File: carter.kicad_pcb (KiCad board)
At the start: 2 copper layers, 45 x 41 mm, 14 parts, among them J1 USB C, J2 Micro_SD_Card, U1 CH340C

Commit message: near v1
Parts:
- added C2: 0.1uF, Capacitor_SMD:C_0603_1608Metric, F.Cu at (148.7, 87.5)
- R3, R4, R5, R6, R7: footprint Resistor_SMD:R_0603_1608Metric -> Resistor_SMD:R_0805_2012Metric
- R8: value R -> 220
- U2: footprint LeapFrog:LeapFrog-Cart -> LeapFrog:Cartridge
- moved U2 42.5 mm to (152.5, 55.0)
- moved D1 36.1 mm to (153.7, 97.0)
- moved J1 34.5 mm to (141.3, 96.9), turned to 0 degrees
- moved R2 33.5 mm to (135.0, 90.0), turned to 180 degrees
- moved C1 26.4 mm to (141.8, 80.0), turned to 180 degrees
- moved J2 23.3 mm to (163.2, 89.8), turned to 0 degrees
- moved R1 21.9 mm to (147.6, 90.0)
- moved R8 11.0 mm to (149.7, 97.0)
- moved R3 10.3 mm to (170.5, 77.5), turned to 180 degrees
- moved U1 10.3 mm to (141.8, 85.0)
- moved R4 9.23 mm to (166.4, 76.5), turned to 180 degrees
- moved R5 7.98 mm to (165.4, 80.0), turned to 180 degrees
- moved R6 7.24 mm to (159.6, 77.5)
- moved R7 5.76 mm to (158.2, 81.2)
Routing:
- net GND: track 0.00 -> 43.7 mm, vias 0 -> 14
- net /SD_D0: track 0.00 -> 35.2 mm
- net /SD_D3: track 0.00 -> 32.2 mm
- net /SD_D2: track 0.00 -> 30.8 mm, vias 0 -> 2
- net /SD_CMD: track 0.00 -> 30.6 mm
- net /SD_CLK: track 0.00 -> 29.9 mm
- net /SD_D1: track 0.00 -> 29.7 mm
- net +3V3: track 0.00 -> 17.4 mm
- net Net-(J1-CC1): track 0.00 -> 6.72 mm
- net Net-(J1-CC2): track 0.00 -> 6.40 mm
- net Net-(U1-UD+): track 8.83 -> 12.5 mm
- net Net-(D1-K): track 0.00 -> 2.43 mm
- net Net-(U1-TXD): track 31.3 -> 33.0 mm
- net Net-(U1-RXD): track 31.3 -> 33.0 mm
- net Net-(U1-UD-): track 12.0 -> 11.0 mm
- added copper zone on F.Cu, net +3V3
- removed copper zone on F.Cu, net GND
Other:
- board size 45 x 41 mm -> 45 x 50 mm
- board text added: "CARTER"
- board text added: "ON!"

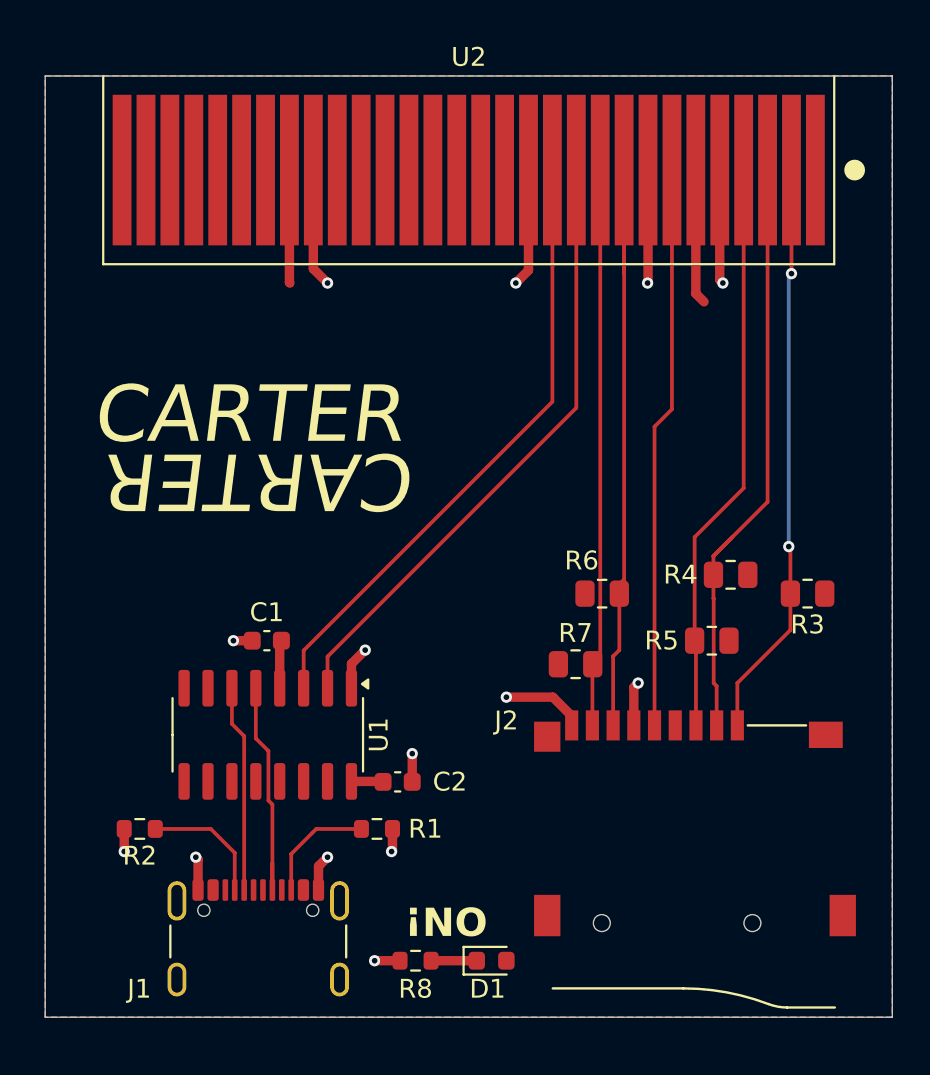
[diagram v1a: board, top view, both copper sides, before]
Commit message: fix: usb-c connectivity
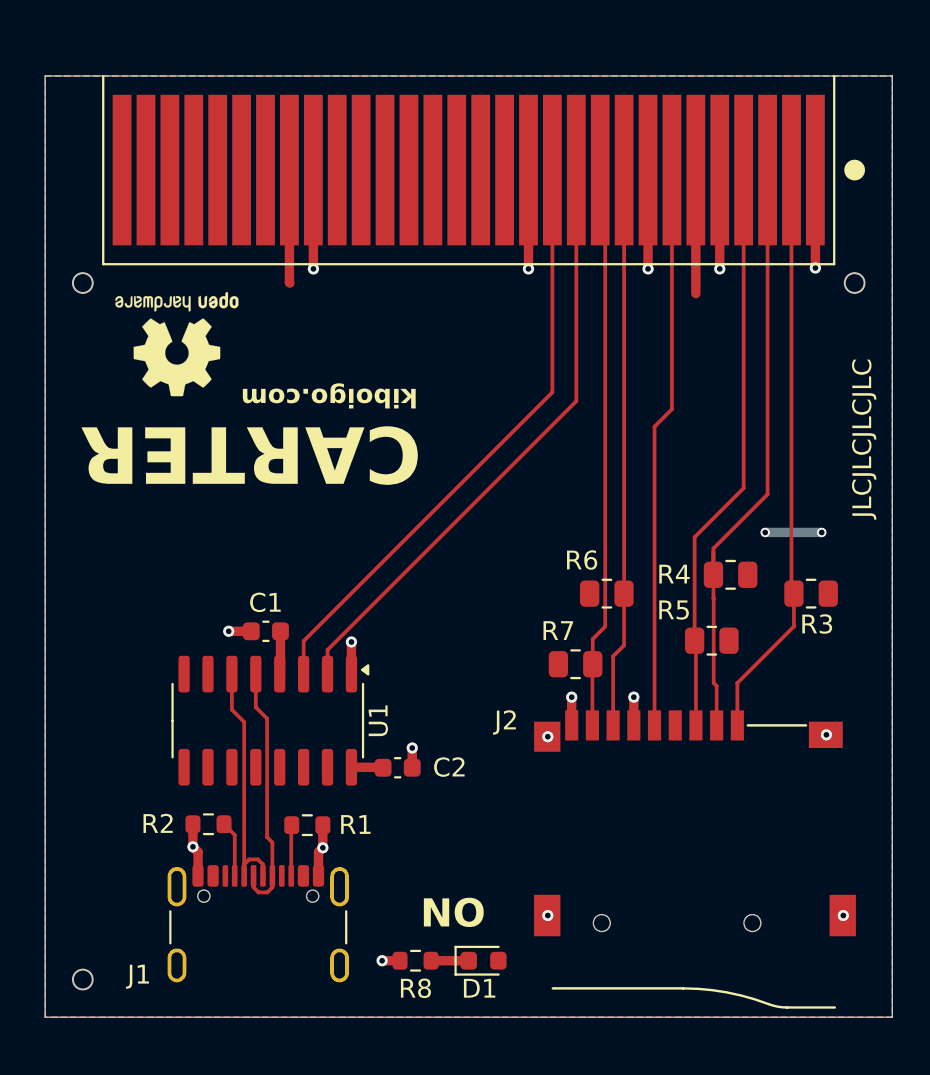
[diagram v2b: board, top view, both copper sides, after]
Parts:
- added REF**: OSHW-Logo2_7.3x6mm_SilkScreen, Symbol:OSHW-Logo2_7.3x6mm_SilkScreen, F.Cu at (137.0, 64.2)
- moved R1 3.71 mm to (143.9, 89.8)
- moved R2 3.66 mm to (138.7, 89.8)
- moved C2 0.75 mm to (148.7, 86.8)
- moved J1 0.75 mm to (141.3, 96.2)
- moved U1 0.75 mm to (141.8, 84.2)
- moved C1 0.50 mm to (141.7, 79.5)
- moved D1 0.43 mm to (153.3, 97.0)
- moved R6 0.25 mm to (159.8, 77.5)
- moved R3 0.19 mm to (170.7, 77.5)
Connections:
- U2 pad 30: (no net) -> GND
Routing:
- net /SD_D0: track 35.2 -> 30.1 mm
- net Net-(J1-CC1): track 6.72 -> 2.98 mm
- net Net-(J1-CC2): track 6.40 -> 2.66 mm
- net GND: track 43.7 -> 40.7 mm, vias 14 -> 17
- net Net-(U1-UD-): track 11.0 -> 13.4 mm
- net +3V3: track 17.4 -> 19.6 mm, vias 0 -> 2
- net Net-(U1-UD+): track 12.5 -> 13.5 mm
- net Net-(U1-TXD): track 33.0 -> 32.2 mm
- net Net-(U1-RXD): track 33.0 -> 32.2 mm
- net /SD_D2: track 30.8 -> 31.2 mm, vias 2 -> 0
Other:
- outline, holes or cut-outs redrawn
- board text added: "JLCJLCJLCJLC"
- board text added: "ON"
- board text added: "kiboigo.com"
- board text added: "we can shrink this by ~6 mm. (44mm)"
- board text removed: "ON!"

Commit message: redesign with ams1117-3.3
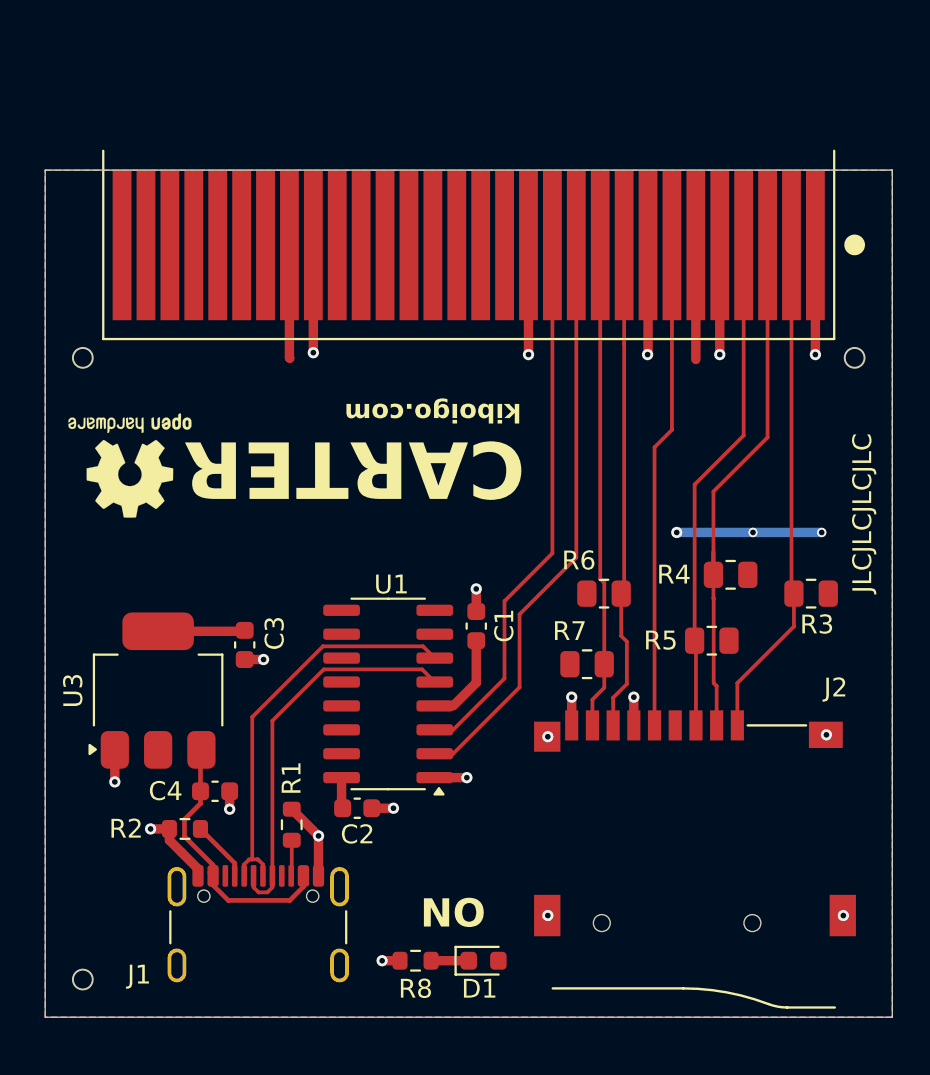
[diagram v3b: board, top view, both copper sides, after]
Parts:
- added C3: 22uF, Capacitor_SMD:C_0603_1608Metric, F.Cu at (140.6, 80.2)
- added C4: 0.1uF, Capacitor_SMD:C_0603_1608Metric, F.Cu at (139.0, 88.0)
- added U3: AMS1117-3.3, Package_TO_SOT_SMD:SOT-223-3_TabPin2, F.Cu at (136.0, 82.7)
- moved C1 11.2 mm to (152.9, 79.2), turned to 90 degrees
- moved REF** 6.92 mm to (134.5, 70.7)
- moved U1 6.55 mm to (148.2, 82.8), turned to 180 degrees
- moved U2 3.98 mm to (152.5, 59.0)
- moved C2 3.04 mm to (146.6, 88.9)
- moved R2 1.27 mm to (137.4, 90.0)
- moved R1 0.83 mm to (143.1, 89.8), turned to 90 degrees
- moved R7 0.61 mm to (158.8, 81.2)
- moved R6 0.15 mm to (159.7, 77.5)
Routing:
- net +5V: track 0.00 -> 15.1 mm
- net +3V3: track 19.6 -> 30.1 mm, vias 2 -> 3
- net GND: track 40.7 -> 50.2 mm, vias 17 -> 20
- net Net-(U1-UD+): track 13.5 -> 21.8 mm
- net Net-(U1-UD-): track 13.4 -> 21.5 mm
- net /SD_CMD: track 30.6 -> 26.6 mm
- net /SD_D2: track 31.2 -> 27.2 mm
- net /SD_CLK: track 29.9 -> 25.9 mm
- net /SD_D3: track 32.0 -> 28.0 mm
- net /SD_D0: track 30.1 -> 26.4 mm
- net /SD_D1: track 29.9 -> 26.3 mm
- net Net-(U1-RXD): track 32.2 -> 28.9 mm
- net Net-(U1-TXD): track 32.2 -> 30.7 mm
- net Net-(J1-CC2): track 2.66 -> 1.95 mm
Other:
- board size 45 x 50 mm -> 45 x 45 mm
- board text removed: "we can shrink this by ~6 mm. (44mm)"
